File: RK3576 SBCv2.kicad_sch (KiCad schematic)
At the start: 0 parts

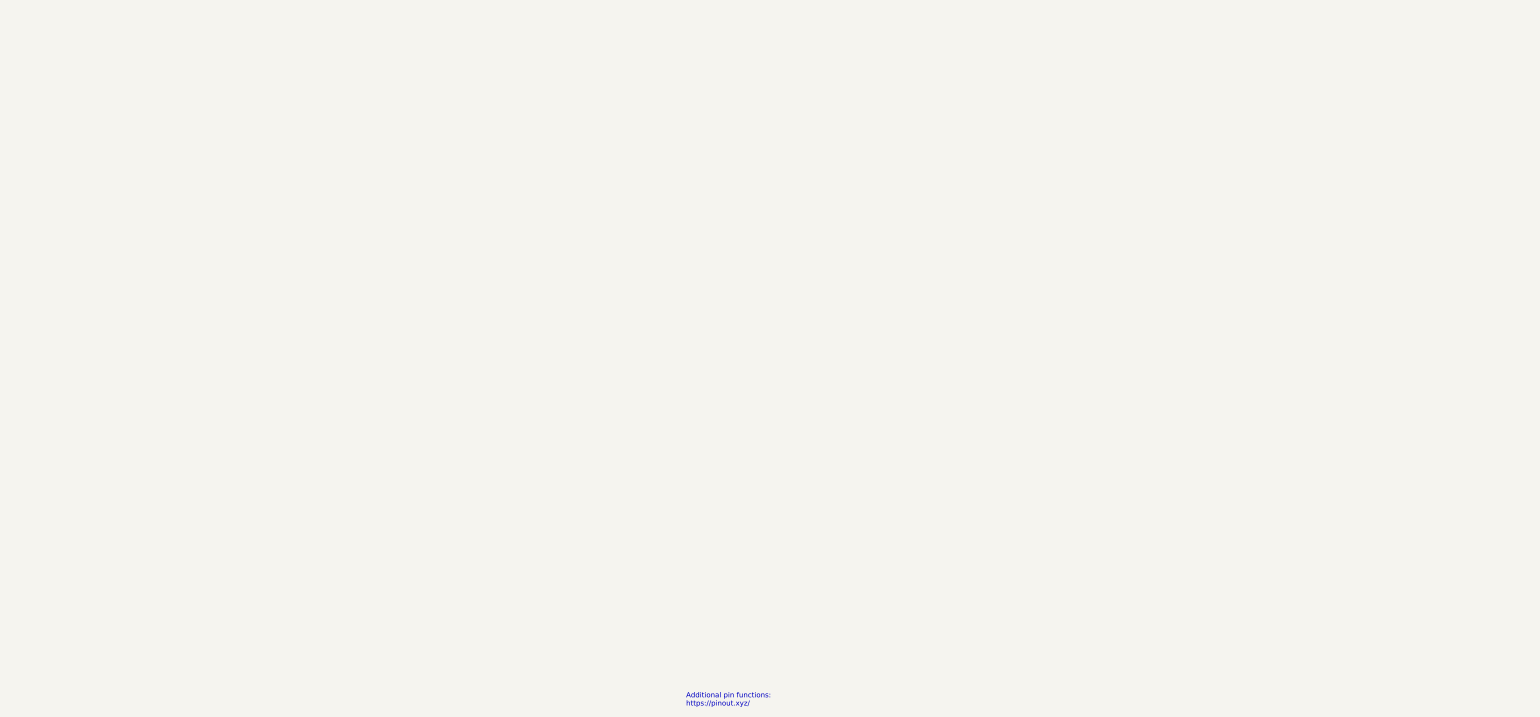
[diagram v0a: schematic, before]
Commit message: Relink hierarchical root: 18 sheets into RK3576 SBCv2 top level
Root was empty (no sheet boxes); all subsheets orphaned.
Rebuilt A1 top level linking RK3576, LPDDR5, Power, Ethernet,
HDMI, MIPI, PCIe, USB-A/C, Wireless, RTC, uSD, GPIO, OLED,
RP2350A, Connectors, Fixtures, DC_Power. block_diagrame kept
docs-only (unlinked, avoids double-instantiation). Lowercase
stub duplicates excluded. ERC: 1388 -> 770 violations.
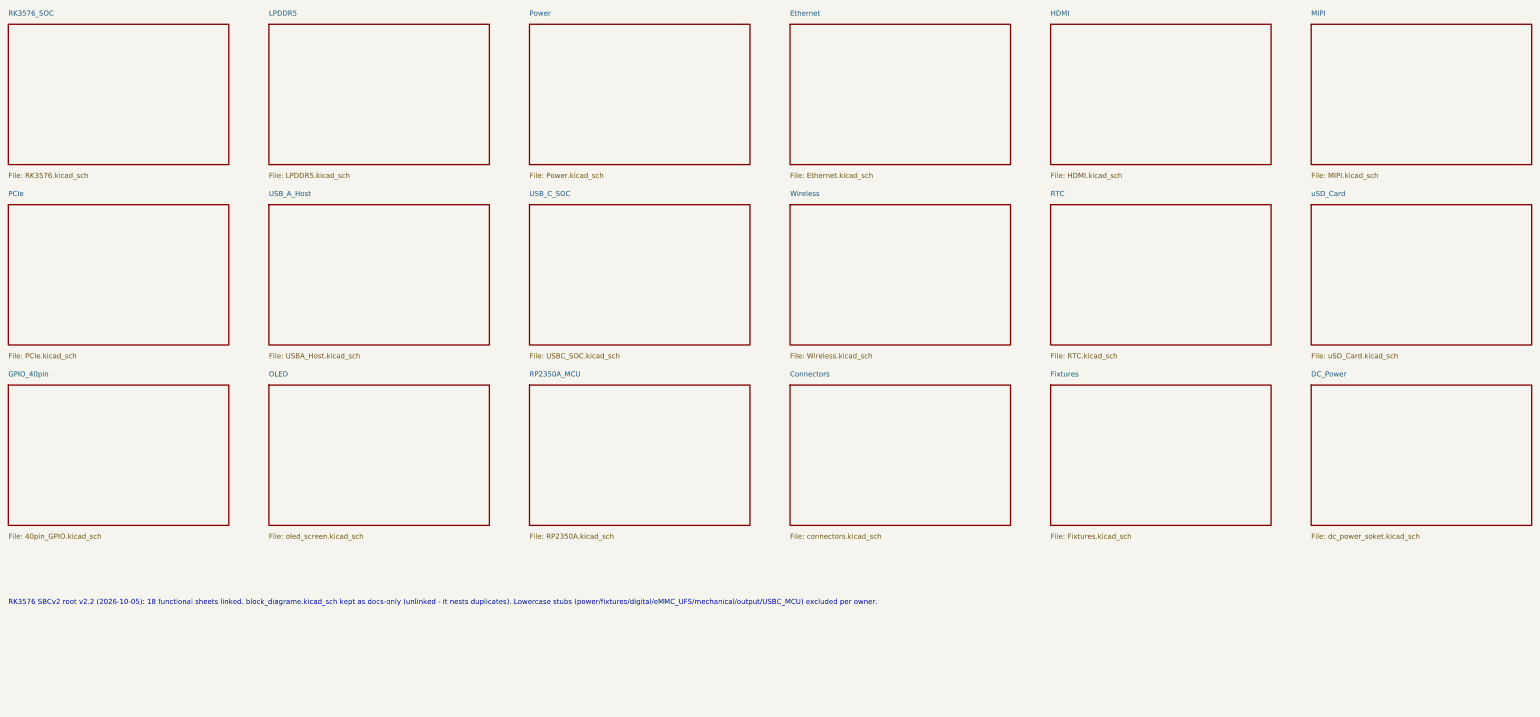
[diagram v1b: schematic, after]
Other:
- added sheet Connectors (connectors.kicad_sch)
- added sheet DC_Power (dc_power_soket.kicad_sch)
- added sheet Ethernet (Ethernet.kicad_sch)
- added sheet Fixtures (Fixtures.kicad_sch)
- added sheet GPIO_40pin (40pin_GPIO.kicad_sch)
- added sheet HDMI (HDMI.kicad_sch)
- added sheet LPDDR5 (LPDDR5.kicad_sch)
- added sheet MIPI (MIPI.kicad_sch)
- added sheet OLED (oled_screen.kicad_sch)
- added sheet PCIe (PCIe.kicad_sch)
- added sheet Power (Power.kicad_sch)
- added sheet RK3576_SOC (RK3576.kicad_sch)
- added sheet RP2350A_MCU (RP2350A.kicad_sch)
- added sheet RTC (RTC.kicad_sch)
- added sheet USB_A_Host (USBA_Host.kicad_sch)
- added sheet USB_C_SOC (USBC_SOC.kicad_sch)
- added sheet Wireless (Wireless.kicad_sch)
- added sheet uSD_Card (uSD_Card.kicad_sch)
- note added: "RK3576 SBCv2 root v2.2 (2026-10-05): 18 functional sheets linked. block_diagrame.kicad_sch kept as docs-only (unlinked - it nests duplicates). Lowercase stubs (power/fixtures/digital/eMMC_UFS/mechanical/output/USBC_MCU) excluded per owner."
- note removed: "Additional pin functions: https://pinout.xyz/"
- title: (none) -> RK3576 SBCv2 - Top Level
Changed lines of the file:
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@@
 	(generator "eeschema")
 	(generator_version "10.0")
-	(paper "A4")
-	(title_block
-		(date "15 nov 2012")
+	(paper "A1")
+	(title_block (title "RK3576 SBCv2 - Top Level") (date "2026-10-05") (rev "v2.2-root-relink"))
+	(sheet (at 10 10) (size 55 35)
+		(fields_autoplaced yes)
+		(stroke (width 0.1524) (type solid))
+		(fill (color 0 0 0 0.0000))
+		(property "Sheet name" "RK3576_SOC" (at 10 8 0) (effects (font (size 1.27 1.27)) (justify left bottom)))
+		(property "Sheet file" "RK3576.kicad_sch" (at 10 47 0) (effects (font (size 1.27 1.27)) (justify left top)))
 	)
-	(text "Additional pin functions:\nhttps://pinout.xyz/"
-		(exclude_from_sim no)
-		(at 179.07 180.34 0)
-		(effects
-			(font
-				(size 1.27 1.27)
-			)
-			(justify left bottom)
-		)
+	(sheet (at 75 10) (size 55 35)
+		(fields_autoplaced yes)
+		(stroke (width 0.1524) (type solid))
+		(fill (color 0 0 0 0.0000))
+		(property "Sheet name" "LPDDR5" (at 75 8 0) (effects (font (size 1.27 1.27)) (justify left bottom)))
+		(property "Sheet file" "LPDDR5.kicad_sch" (at 75 47 0) (effects (font (size 1.27 1.27)) (justify left top)))
 	)
-	(sheet_instances
-		(path "/"
-			(page "2")
-		)
+	(sheet (at 140 10) (size 55 35)
+		(fields_autoplaced yes)
+		(stroke (width 0.1524) (type solid))
+		(fill (color 0 0 0 0.0000))
+		(property "Sheet name" "Power" (at 140 8 0) (effects (font (size 1.27 1.27)) (justify left bottom)))
+		(property "Sheet file" "Power.kicad_sch" (at 140 47 0) (effects (font (size 1.27 1.27)) (justify left top)))
 	)
+	(sheet (at 205 10) (size 55 35)
+		(fields_autoplaced yes)
+		(stroke (width 0.1524) (type solid))
+		(fill (color 0 0 0 0.0000))
+		(property "Sheet name" "Ethernet" (at 205 8 0) (effects (font (size 1.27 1.27)) (justify left bottom)))
+		(property "Sheet file" "Ethernet.kicad_sch" (at 205 47 0) (effects (font (size 1.27 1.27)) (justify left top)))
+	)
+	(sheet (at 270 10) (size 55 35)
+		(fields_autoplaced yes)
+		(stroke (width 0.1524) (type solid))
+		(fill (color 0 0 0 0.0000))
+		(property "Sheet name" "HDMI" (at 270 8 0) (effects (font (size 1.27 1.27)) (justify left bottom)))
+		(property "Sheet file" "HDMI.kicad_sch" (at 270 47 0) (effects (font (size 1.27 1.27)) (justify left top)))
+	)
+	(sheet (at 335 10) (size 55 35)
+		(fields_autoplaced yes)
+		(stroke (width 0.1524) (type solid))
+		(fill (color 0 0 0 0.0000))
+		(property "Sheet name" "MIPI" (at 335 8 0) (effects (font (size 1.27 1.27)) (justify left bottom)))
+		(property "Sheet file" "MIPI.kicad_sch" (at 335 47 0) (effects (font (size 1.27 1.27)) (justify left top)))
+	)
+	(sheet (at 10 55) (size 55 35)
+		(fields_autoplaced yes)
+		(stroke (width 0.1524) (type solid))
+		(fill (color 0 0 0 0.0000))
+		(property "Sheet name" "PCIe" (at 10 53 0) (effects (font (size 1.27 1.27)) (justify left bottom)))
+		(property "Sheet file" "PCIe.kicad_sch" (at 10 92 0) (effects (font (size 1.27 1.27)) (justify left top)))
+	)
+	(sheet (at 75 55) (size 55 35)
+		(fields_autoplaced yes)
+		(stroke (width 0.1524) (type solid))
+		(fill (color 0 0 0 0.0000))
+		(property "Sheet name" "USB_A_Host" (at 75 53 0) (effects (font (size 1.27 1.27)) (justify left bottom)))
+		(property "Sheet file" "USBA_Host.kicad_sch" (at 75 92 0) (effects (font (size 1.27 1.27)) (justify left top)))
+	)
+	(sheet (at 140 55) (size 55 35)
+		(fields_autoplaced yes)
+		(stroke (width 0.1524) (type solid))
+		(fill (color 0 0 0 0.0000))
+		(property "Sheet name" "USB_C_SOC" (at 140 53 0) (effects (font (size 1.27 1.27)) (justify left bottom)))
+		(property "Sheet file" "USBC_SOC.kicad_sch" (at 140 92 0) (effects (font (size 1.27 1.27)) (justify left top)))
+	)
+	(sheet (at 205 55) (size 55 35)
+		(fields_autoplaced yes)
+		(stroke (width 0.1524) (type solid))
+		(fill (color 0 0 0 0.0000))
+		(property "Sheet name" "Wireless" (at 205 53 0) (effects (font (size 1.27 1.27)) (justify left bottom)))
+		(property "Sheet file" "Wireless.kicad_sch" (at 205 92 0) (effects (font (size 1.27 1.27)) (justify left top)))
+	)
+	(sheet (at 270 55) (size 55 35)
+		(fields_autoplaced yes)
+		(stroke (width 0.1524) (type solid))
+		(fill (color 0 0 0 0.0000))
+		(property "Sheet name" "RTC" (at 270 53 0) (effects (font (size 1.27 1.27)) (justify left bottom)))
+		(property "Sheet file" "RTC.kicad_sch" (at 270 92 0) (effects (font (size 1.27 1.27)) (justify left top)))
+	)
+	(sheet (at 335 55) (size 55 35)
+		(fields_autoplaced yes)
+		(stroke (width 0.1524) (type solid))
+		(fill (color 0 0 0 0.0000))
+		(property "Sheet name" "uSD_Card" (at 335 53 0) (effects (font (size 1.27 1.27)) (justify left bottom)))
+		(property "Sheet file" "uSD_Card.kicad_sch" (at 335 92 0) (effects (font (size 1.27 1.27)) (justify left top)))
+	)
+	(sheet (at 10 100) (size 55 35)
+		(fields_autoplaced yes)
+		(stroke (width 0.1524) (type solid))
+		(fill (color 0 0 0 0.0000))
+		(property "Sheet name" "GPIO_40pin" (at 10 98 0) (effects (font (size 1.27 1.27)) (justify left bottom)))
+		(property "Sheet file" "40pin_GPIO.kicad_sch" (at 10 137 0) (effects (font (size 1.27 1.27)) (justify left top)))
+	)
+	(sheet (at 75 100) (size 55 35)
+		(fields_autoplaced yes)
+		(stroke (width 0.1524) (type solid))
+		(fill (color 0 0 0 0.0000))
+		(property "Sheet name" "OLED" (at 75 98 0) (effects (font (size 1.27 1.27)) (justify left bottom)))
+		(property "Sheet file" "oled_screen.kicad_sch" (at 75 137 0) (effects (font (size 1.27 1.27)) (justify left top)))
+	)
+	(sheet (at 140 100) (size 55 35)
+		(fields_autoplaced yes)
+		(stroke (width 0.1524) (type solid))
+		(fill (color 0 0 0 0.0000))
+		(property "Sheet name" "RP2350A_MCU" (at 140 98 0) (effects (font (size 1.27 1.27)) (justify left bottom)))
+		(property "Sheet file" "RP2350A.kicad_sch" (at 140 137 0) (effects (font (size 1.27 1.27)) (justify left top)))
+	)
+	(sheet (at 205 100) (size 55 35)
+		(fields_autoplaced yes)
+		(stroke (width 0.1524) (type solid))
+		(fill (color 0 0 0 0.0000))
+		(property "Sheet name" "Connectors" (at 205 98 0) (effects (font (size 1.27 1.27)) (justify left bottom)))
+		(property "Sheet file" "connectors.kicad_sch" (at 205 137 0) (effects (font (size 1.27 1.27)) (justify left top)))
+	)
+	(sheet (at 270 100) (size 55 35)
+		(fields_autoplaced yes)
+		(stroke (width 0.1524) (type solid))
+		(fill (color 0 0 0 0.0000))
+		(property "Sheet name" "Fixtures" (at 270 98 0) (effects (font (size 1.27 1.27)) (justify left bottom)))
+		(property "Sheet file" "Fixtures.kicad_sch" (at 270 137 0) (effects (font (size 1.27 1.27)) (justify left top)))
+	)
+	(sheet (at 335 100) (size 55 35)
+		(fields_autoplaced yes)
+		(stroke (width 0.1524) (type solid))
+		(fill (color 0 0 0 0.0000))
+		(property "Sheet name" "DC_Power" (at 335 98 0) (effects (font (size 1.27 1.27)) (justify left bottom)))
+		(property "Sheet file" "dc_power_soket.kicad_sch" (at 335 137 0) (effects (font (size 1.27 1.27)) (justify left top)))
+	)
+	(text "RK3576 SBCv2 root v2.2 (2026-10-05): 18 functional sheets linked. block_diagrame.kicad_sch kept as docs-only (unlinked - it nests duplicates). Lowercase stubs (power/fixtures/digital/eMMC_UFS/mechanical/output/USBC_MCU) excluded per owner."
+		(exclude_from_sim no) (at 10 155 0) (effects (font (size 1.27 1.27)) (justify left bottom))
+	)
+	(sheet_instances (path "/" (page "1")))
 	(embedded_fonts no)
 )
